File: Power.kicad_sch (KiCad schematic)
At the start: 52 parts, among them J2 USB-C, J3 JST-PH-2, J6 JST-PH-2, Q1 FS8205A, SW1 SLIDE_SWITCH, U2 DW01A, U3 TPS61220, U5 TPS60403, U6 ADP7142AUJZ-5.0, U7 MCP73831T, U8 ADP7182-5.0

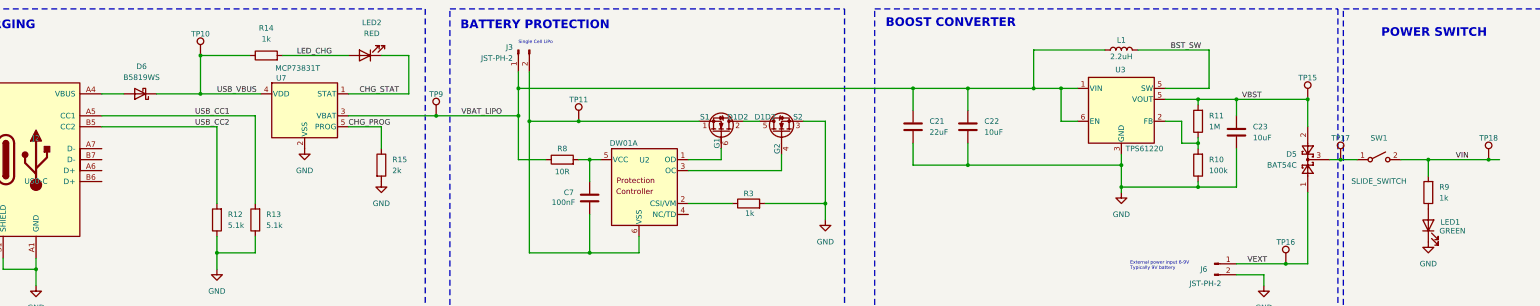
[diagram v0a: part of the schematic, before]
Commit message: DRC completed. Need to add some 3D models.
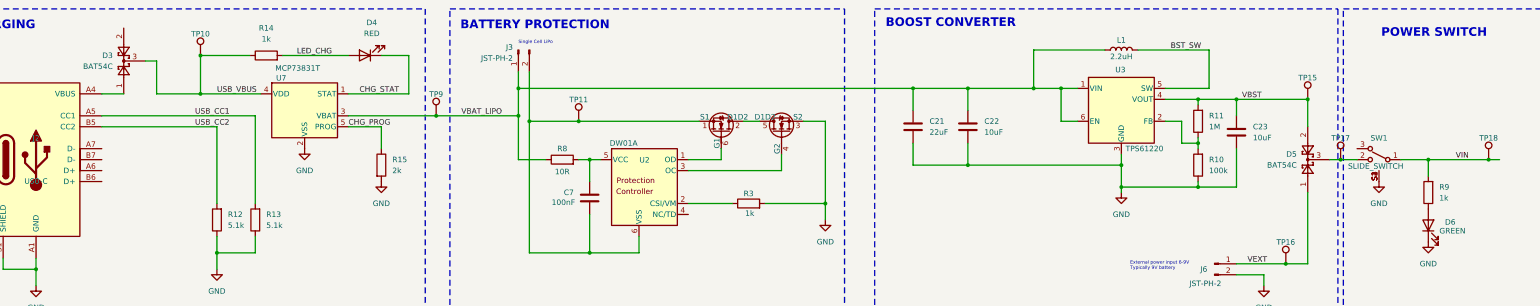
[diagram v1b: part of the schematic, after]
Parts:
- removed D6: B5819WS, Diode_SMD:D_SOD-323, symbol Device:D_Schottky
- added D3: BAT54C, Package_TO_SOT_SMD:SOT-23, symbol Diode:BAT54C
- C12, C16, C22, C23: footprint Capacitor_SMD:C_0805_2012Metric -> Capacitor_SMD:C_0603_1608Metric_Pad1.08x0.95mm_HandSolder
- C15, C18, C19, C20, C7: footprint Capacitor_SMD:C_0603_1608Metric -> Capacitor_SMD:C_0402_1005Metric_Pad0.74x0.62mm_HandSolder
- C21: footprint Capacitor_SMD:C_1206_3216Metric -> Capacitor_SMD:C_0805_2012Metric_Pad1.18x1.45mm_HandSolder
- L1: footprint Inductor_SMD:L_3015_3815Metric -> Inductor_SMD:L_Changjiang_FTC303010D
- Q1: footprint (none) -> Package_TO_SOT_SMD:TSOT-23-6
- R10, R11, R12, R13, R14, R15, R9: footprint Resistor_SMD:R_0603_1608Metric -> Resistor_SMD:R_0402_1005Metric_Pad0.72x0.64mm_HandSolder
- R8: footprint Resistor_SMD:R_0402_1005Metric -> Resistor_SMD:R_0402_1005Metric_Pad0.72x0.64mm_HandSolder
- SW1: footprint Button_Switch_SMD:SW_SPST_CK_RS282G05A3 -> ProjectLib:SW_PCM12SMTR
- TP10, TP11, TP12, TP13, TP14, TP15, TP16, TP17, TP18, TP19, TP20, TP9: footprint TestPoint:TestPoint_Pad_D1.5mm -> TestPoint:TestPoint_Pad_D1.0mm
- renumbered LED2 to D4, LED1 to D6
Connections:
- net GND: now also SW1.S1, SW1.S2, SW1.S3, SW1.S4; no longer U6.9 (GND)
- net USB_VBUS: now also D3.3
- net VBST: now also U3.4 (VOUT); no longer U3.5 (VOUT)
- net VIN: now also SW1.1 (A); no longer SW1.2 (B)
- net at D5.3, TP17.1: now also SW1.2 (B); no longer SW1.1 (A)
- net at J2.A4 (VBUS), J2.A9 (VBUS), J2.B4 (VBUS)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: now also D3.1

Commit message: R1 sent to JLCPCB
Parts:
- C11, C13, C14, C17, C8: JLCPCB# (none) -> C59782
- C12, C16, C22, C23: JLCPCB# (none) -> C237435
- C15, C18, C19, C7: JLCPCB# (none) -> C60474
- C20: JLCPCB# (none) -> C15195
- C21: JLCPCB# (none) -> C296720
- D3, D5: JLCPCB# (none) -> C2135
- D4: JLCPCB# (none) -> C2295
- D6: JLCPCB# (none) -> C2297
- J2: JLCPCB# (none) -> C165948
- J3, J6: JLCPCB# (none) -> C173752
- L1: JLCPCB# (none) -> C136233
- Q1: JLCPCB# (none) -> C2830320
- R10: JLCPCB# (none) -> C25741
- R11: JLCPCB# (none) -> C26083
- R12, R13: JLCPCB# (none) -> C25905
- R14, R3, R9: JLCPCB# (none) -> C11702
- R15: JLCPCB# (none) -> C4109
- R8: JLCPCB# (none) -> C25077
- SW1: JLCPCB# (none) -> C221841; MPN OS102011MA1QN1 -> PCM12SMTR
- TP10, TP11, TP12, TP13, TP14, TP15, TP16, TP17, TP18, TP19, TP20, TP9: now left out of the parts list
- U2: JLCPCB# (none) -> C2927799
- U3: JLCPCB# (none) -> C15421
- U5: JLCPCB# (none) -> C11338
- U6: JLCPCB# (none) -> C659367
- U7: JLCPCB# (none) -> C424093
- U8: JLCPCB# (none) -> C514357
